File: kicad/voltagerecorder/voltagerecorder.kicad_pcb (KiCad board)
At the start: 2 copper layers, 70.1 x 47.2 mm, 107 parts, among them J1 Conn_02x10_Odd_Even, J2 Phoenix Stecker, J3 Conn_01x08, J4 Conn_01x01_Male, J5 Conn_01x01_Male, J6 Conn_01x01_Male, J7 Conn_01x01_Male, J8 Conn_01x02, J9 USB_C_Receptacle_USB2.0, P1 DM3CS-SF, U1 Opamp_Quad, U2 DCDC_BIPOLAR, U3 L78L12ACUTR, U4 L79L12ACUTR, U5 ADS8638, U6 STM32G473CBT6, U7 L78L12ACUTR, U8 ESP32-C3-WROOM-02, Y1 Crystal_GND23

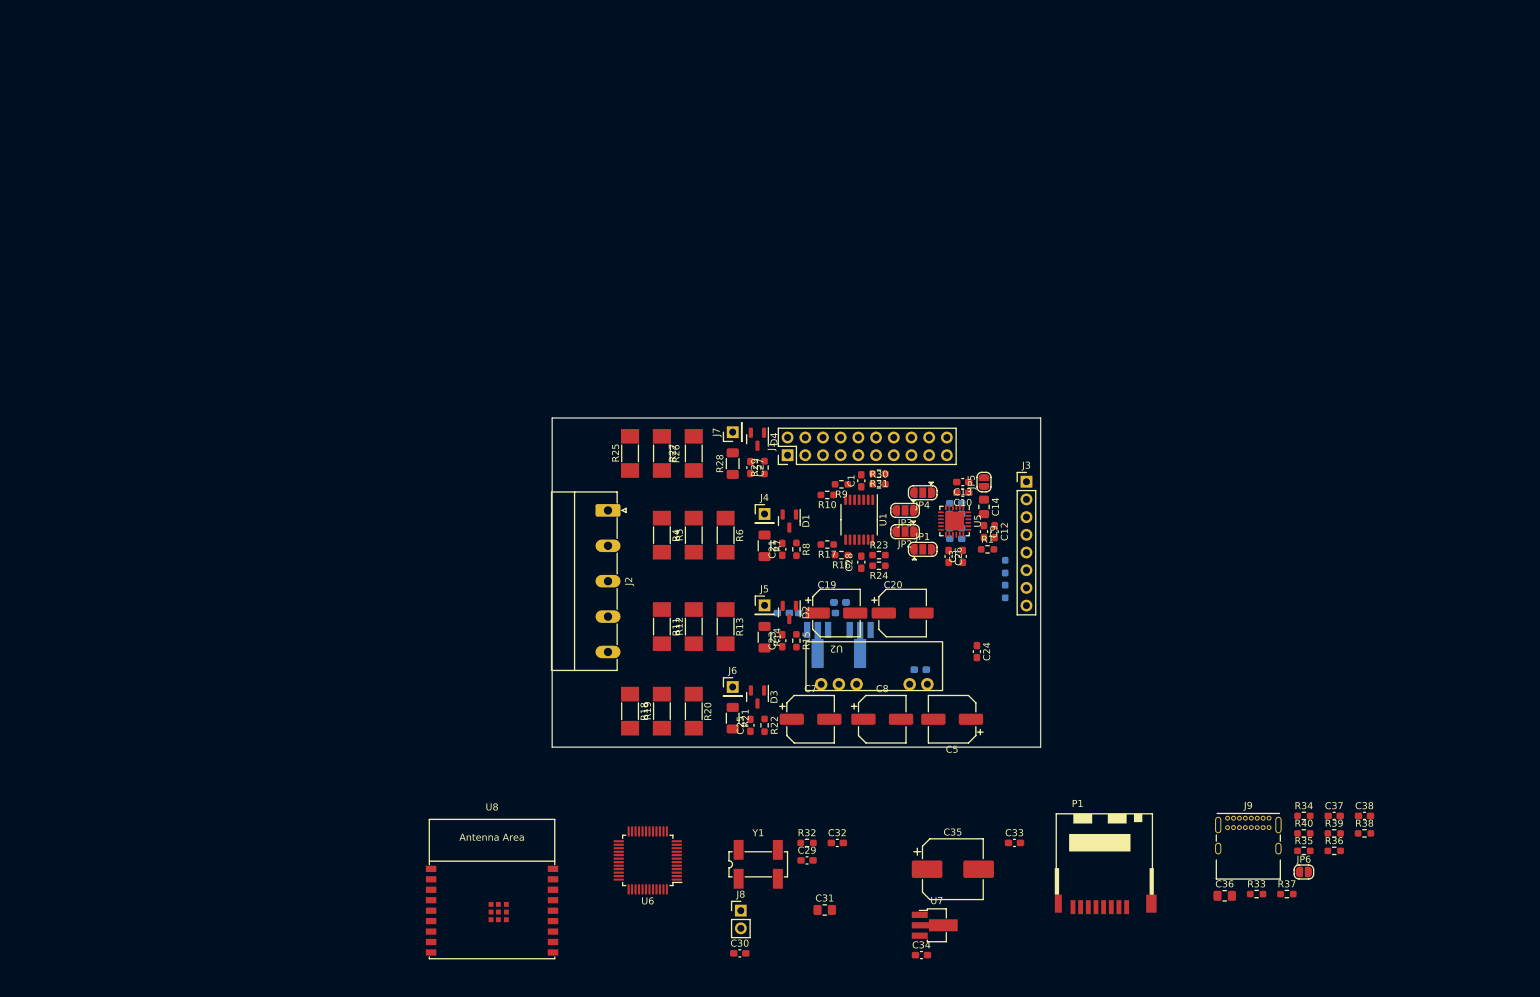
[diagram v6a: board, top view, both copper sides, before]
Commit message: vor entfernung von g4
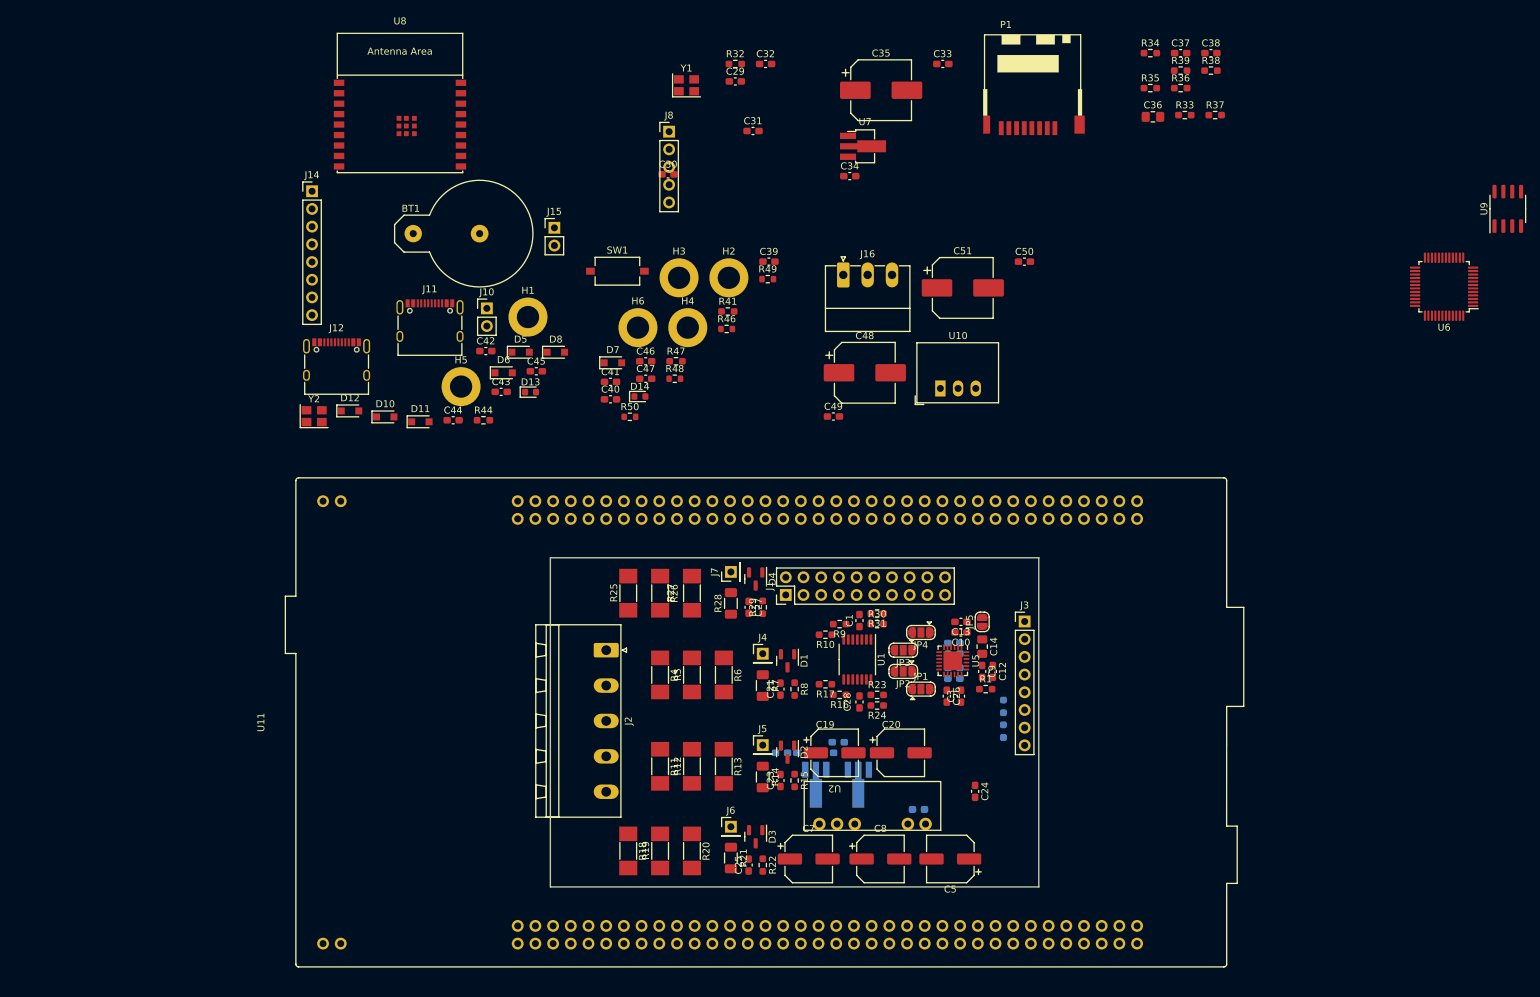
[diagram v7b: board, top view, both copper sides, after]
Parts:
- removed J9: USB_C_Receptacle_USB2.0, Connector_USB:USB_C_Receptacle_GCT_USB4085
- removed JP6: SolderJumper_2_Open, Jumper:SolderJumper-2_P1.3mm_Open_RoundedPad1.0x1.5mm
- removed R40: 15k, Resistor_SMD:R_0603_1608Metric_Pad0.98x0.95mm_HandSolder
- added BT1: Battery_Cell, Battery:BatteryHolder_Keystone_500, F.Cu at (89.8, 52.3)
- added C39: 100n, Capacitor_SMD:C_0603_1608Metric_Pad1.08x0.95mm_HandSolder, F.Cu at (140.8, 56.3)
- added C40: 1u, Capacitor_SMD:C_0603_1608Metric_Pad1.08x0.95mm_HandSolder, F.Cu at (118.1, 76.1)
- added C41: 22pF, Capacitor_SMD:C_0603_1608Metric_Pad1.08x0.95mm_HandSolder, F.Cu at (118.1, 73.5)
- added C42: 22pF, Capacitor_SMD:C_0603_1608Metric_Pad1.08x0.95mm_HandSolder, F.Cu at (100.2, 69.1)
- added C43: 22pF, Capacitor_SMD:C_0603_1608Metric_Pad1.08x0.95mm_HandSolder, F.Cu at (102.4, 75.0)
- added C44: 22pF, Capacitor_SMD:C_0603_1608Metric_Pad1.08x0.95mm_HandSolder, F.Cu at (95.5, 79.1)
- added C45: 100n, Capacitor_SMD:C_0603_1608Metric_Pad1.08x0.95mm_HandSolder, F.Cu at (107.5, 72.0)
- added C46: 10nF, Capacitor_SMD:C_0603_1608Metric_Pad1.08x0.95mm_HandSolder, F.Cu at (123.1, 70.6)
- added C47: 10nF, Capacitor_SMD:C_0603_1608Metric_Pad1.08x0.95mm_HandSolder, F.Cu at (123.1, 73.1)
- added C48: 470u, Capacitor_SMD:CP_Elec_8x10.5, F.Cu at (154.6, 72.2)
- added C49: 10u, Capacitor_SMD:C_0603_1608Metric_Pad1.08x0.95mm_HandSolder, F.Cu at (150.1, 78.5)
- added C50: 10u, Capacitor_SMD:C_0603_1608Metric_Pad1.08x0.95mm_HandSolder, F.Cu at (177.5, 56.3)
- added C51: 470u, Capacitor_SMD:CP_Elec_8x10.5, F.Cu at (168.7, 60.1)
- added D10: D_Zener, Diode_SMD:D_SOD-323_HandSoldering, F.Cu at (85.8, 78.6)
- added D11: D_Zener, Diode_SMD:D_SOD-323_HandSoldering, F.Cu at (90.8, 79.3)
- added D12: D_Zener, Diode_SMD:D_SOD-323_HandSoldering, F.Cu at (80.7, 77.7)
- added D13: RED, Diode_SMD:D_0603_1608Metric, F.Cu at (106.6, 75.0)
- added D14: GREEN, Diode_SMD:D_0603_1608Metric, F.Cu at (122.3, 75.7)
- added D5: D_Zener, Diode_SMD:D_SOD-323_HandSoldering, F.Cu at (105.2, 69.3)
- added D6: D_Zener, Diode_SMD:D_SOD-323_HandSoldering, F.Cu at (102.8, 72.3)
- added D7: D_Zener, Diode_SMD:D_SOD-323_HandSoldering, F.Cu at (118.4, 70.8)
- added D8: D_Zener, Diode_SMD:D_SOD-323_HandSoldering, F.Cu at (110.3, 69.3)
- added H1: MountingHole_Pad, MountingHole:MountingHole_3.2mm_M3_DIN965_Pad, F.Cu at (106.3, 64.3)
- added H2: MountingHole_Pad, MountingHole:MountingHole_3.2mm_M3_DIN965_Pad, F.Cu at (135.1, 58.6)
- added H3: MountingHole_Pad, MountingHole:MountingHole_3.2mm_M3_DIN965_Pad, F.Cu at (127.9, 58.6)
- added H4: MountingHole_Pad, MountingHole:MountingHole_3.2mm_M3_DIN965_Pad, F.Cu at (129.2, 65.8)
- added H5: MountingHole_Pad, MountingHole:MountingHole_3.2mm_M3_DIN965_Pad, F.Cu at (96.7, 74.2)
- added H6: MountingHole_Pad, MountingHole:MountingHole_3.2mm_M3_DIN965_Pad, F.Cu at (122.0, 65.8)
- added J10: Conn_01x02, Connector_PinHeader_2.54mm:PinHeader_1x02_P2.54mm_Vertical, F.Cu at (100.4, 63.0)
- added J11: USB_C_Receptacle_USB2.0, Connector_USB:USB_C_Receptacle_XKB_U262-16XN-4BVC11, F.Cu at (92.2, 66.0)
- added J12: USB_C_Receptacle_USB2.0, Connector_USB:USB_C_Receptacle_XKB_U262-16XN-4BVC11, F.Cu at (78.8, 71.5)
- added J14: Conn_01x08, Connector_PinHeader_2.54mm:PinHeader_1x08_P2.54mm_Vertical, F.Cu at (75.3, 46.2)
- added J15: Conn_01x02, Connector_PinHeader_2.54mm:PinHeader_1x02_P2.54mm_Vertical, F.Cu at (110.0, 51.4)
- added J16: Conn_01x03, Connector_Phoenix_MC:PhoenixContact_MC_1,5_3-G-3.5_1x03_P3.50mm_Horizontal, F.Cu at (151.5, 58.2)
- added R41: 15k, Resistor_SMD:R_0603_1608Metric_Pad0.98x0.95mm_HandSolder, F.Cu at (134.9, 63.4)
- added R44: 10k, Resistor_SMD:R_0603_1608Metric_Pad0.98x0.95mm_HandSolder, F.Cu at (99.9, 79.1)
- added R46: 1M, Resistor_SMD:R_0603_1608Metric, F.Cu at (134.8, 66.0)
- added R47: 10k, Resistor_SMD:R_0603_1608Metric_Pad0.98x0.95mm_HandSolder, F.Cu at (127.5, 70.6)
- added R48: 1M, Resistor_SMD:R_0603_1608Metric, F.Cu at (127.3, 73.1)
- added R49: 1k, Resistor_SMD:R_0603_1608Metric, F.Cu at (140.7, 58.8)
- added R50: 1k, Resistor_SMD:R_0603_1608Metric, F.Cu at (120.9, 78.6)
- added SW1: SW_Push, Button_Switch_SMD:SW_Tactile_SPST_NO_Straight_CK_PTS636Sx25SMTRLFS, F.Cu at (119.1, 57.7)
- added U10: P78E-1000, Converter_DCDC:Converter_DCDC_RECOM_R-78E-0.5_THT, F.Cu at (165.4, 74.5)
- added U11: NUCLEO144-H743ZI, Module:ST_Morpho_Connector_144_STLink, F.Cu at (104.8, 154.2)
- added U9: ESP-PSRAM32, Package_SO:SOIC-8_3.9x4.9mm_P1.27mm, F.Cu at (246.9, 48.7)
- added Y2: 24MHz, Crystal:Crystal_SMD_3225-4Pin_3.2x2.5mm, F.Cu at (75.6, 78.5)
- C24, C29: value 12p -> 100n
- C31: value 10u -> 1u; footprint Capacitor_SMD:C_0805_2012Metric_Pad1.18x1.45mm_HandSolder -> Capacitor_SMD:C_0603_1608Metric_Pad1.08x0.95mm_HandSolder
- C33, C34: value 100n -> 1u
- J2: value Phoenix Stecker -> Conn_01x05; footprint Connector_Phoenix_MC_HighVoltage:PhoenixContact_MC_1,5_5-G-5.08_1x05_P5.08mm_Horizontal -> Connector_Phoenix_MSTB:PhoenixContact_MSTBA_2,5_5-G-5,08_1x05_P5.08mm_Horizontal
- J8: value Conn_01x02 -> Conn_01x05; footprint Connector_PinHeader_2.54mm:PinHeader_1x02_P2.54mm_Vertical -> Connector_PinHeader_2.54mm:PinHeader_1x05_P2.54mm_Vertical
- R3: value nc -> 10k
- Y1: value Crystal_GND23 -> 32.768kHz; footprint Crystal:Crystal_SMD_SeikoEpson_MC306-4Pin_8.0x3.2mm_HandSoldering -> Crystal:Crystal_SMD_3225-4Pin_3.2x2.5mm
- moved U6 140.9 mm to (237.7, 59.9)
- moved U8 113.6 mm to (87.9, 36.5)
- moved C30 112.3 mm to (126.4, 43.8)
- moved C34 112.3 mm to (152.4, 44.0)
- moved U7 112.3 mm to (154.3, 39.7)
- moved C29 112.3 mm to (136.0, 30.4)
- moved C31 112.3 mm to (138.5, 37.5)
- moved Y1 112.3 mm to (129.0, 31.0)
- moved C32 112.3 mm to (140.4, 27.9)
- moved C33 112.3 mm to (165.8, 27.9)
- moved C35 112.3 mm to (156.9, 31.7)
- moved C36 112.3 mm to (196.0, 35.5)
- moved J8 112.3 mm to (126.5, 37.6)
- moved P1 112.3 mm to (178.7, 30.9)
- moved R32 112.3 mm to (136.0, 27.9)
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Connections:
- C24 pad 1: Net-(C24-Pad1) -> +3.3V
- C29 pad 1: Net-(C29-Pad1) -> +3.3V
- C30 pad 1: Net-(C30-Pad1) -> +3.3V
- C32 pad 1: Net-(C31-Pad1) -> /G4_NRST
- C38 pad 1: Net-(C38-Pad1) -> /BUTTON
- J1 pad 1: /IN0_EXT -> GND
- J1 pad 10: unconnected-(J1-Pad10) -> /REF_EXT
- J1 pad 11: +3.3V -> /IN0_EXT
- J1 pad 12: /REF_EXT -> /IN4_EXT
- J1 pad 13: -15V -> /IN1_EXT
- J1 pad 14: +15V -> /IN5_EXT
- J1 pad 15: -12V -> /IN2_EXT
- J1 pad 16: +12V -> /IN6_EXT
- J1 pad 17: +5V -> /IN3_EXT
- J1 pad 18: +5V -> /IN7_EXT
- J1 pad 19: GND -> /G4_PA4
- J1 pad 2: /IN4_EXT -> GND
- J1 pad 20: GND -> /G4_PA5
- J1 pad 3: /IN1_EXT -> +5V
- J1 pad 4: /IN5_EXT -> +5V
- J1 pad 5: /IN2_EXT -> -12V
- J1 pad 6: /IN6_EXT -> +12V
- J1 pad 7: /IN3_EXT -> -15V
- J1 pad 8: /IN7_EXT -> +15V
- J1 pad 9: unconnected-(J1-Pad9) -> +3.3V
- J8 pad 1: unconnected-(J8-Pad1) -> /ESP_EN
- J8 pad 2: GND -> /ESP_BOOT
- P1 pad 1: Net-(P1-Pad1) -> unconnected-(P1-Pad1)
- P1 pad 2: Net-(P1-Pad2) -> /SPI3_NSS
- P1 pad 3: Net-(P1-Pad3) -> /SPI3_MOSI
- P1 pad 5: Net-(P1-Pad5) -> /SPI3_CLK
- P1 pad 7: Net-(P1-Pad7) -> /SPI3_MISO
- P1 pad 8: Net-(P1-Pad8) -> unconnected-(P1-Pad8)
- R1 pad 2: /MISO -> /SPI2_MISO
- R2 pad 1: /CS -> /SPI2_NSS
- R3 pad 2: /CS -> /BOOT0
- R32 pad 1: Net-(C30-Pad1) -> /G4_NRST
- R33 pad 1: Net-(P1-Pad3) -> /SPI3_MOSI
- R34 pad 1: Net-(P1-Pad5) -> /SPI3_CLK
- R35 pad 1: Net-(P1-Pad7) -> /SPI3_MISO
- R36 pad 1: Net-(P1-Pad8) -> /ESP_BOOT
- R37 pad 1: Net-(P1-Pad1) -> /SENSE_5V
- R37 pad 2: +3.3V -> +5V
- R38 pad 1: Net-(P1-Pad2) -> /SPI3_NSS
- R39 pad 1: Net-(C38-Pad1) -> /BUTTON
- R39 pad 2: +5V -> +3.3V
- U5 pad 16: /CS -> /SPI2_NSS
- U5 pad 17: /SCLK -> /SPI2_CLK
- U5 pad 18: /MOSI -> /SPI2_MOSI
- U5 pad 22: /AL_PD -> /ADC_PD
- U6 pad 1: unconnected-(U6-Pad1) -> Net-(BT1-Pad1)
- U6 pad 10: unconnected-(U6-Pad10) -> /QSPI_NSS
- U6 pad 11: unconnected-(U6-Pad11) -> /QSPI_CLK
- U6 pad 12: unconnected-(U6-Pad12) -> /G4_PA4
- U6 pad 13: unconnected-(U6-Pad13) -> /G4_PA5
- U6 pad 14: unconnected-(U6-Pad14) -> /QSPI_IO3
- U6 pad 15: unconnected-(U6-Pad15) -> /QSPI_IO2
- U6 pad 16: unconnected-(U6-Pad16) -> /QSPI_IO1
- U6 pad 17: unconnected-(U6-Pad17) -> /QSPI_IO0
- U6 pad 18: unconnected-(U6-Pad18) -> /SENSE_5V
- U6 pad 19: unconnected-(U6-Pad19) -> GND
- U6 pad 20: unconnected-(U6-Pad20) -> Net-(C31-Pad1)
- U6 pad 21: unconnected-(U6-Pad21) -> +3.3V
- U6 pad 22: unconnected-(U6-Pad22) -> /UART_G4TX_ESPRX
- U6 pad 23: unconnected-(U6-Pad23) -> GND
- U6 pad 24: unconnected-(U6-Pad24) -> +3.3V
- U6 pad 25: unconnected-(U6-Pad25) -> /UART_G4RX_ESPTX
- U6 pad 26: unconnected-(U6-Pad26) -> /SPI2_NSS
- U6 pad 27: unconnected-(U6-Pad27) -> /SPI2_CLK
- U6 pad 28: unconnected-(U6-Pad28) -> /SPI2_MISO
- U6 pad 29: unconnected-(U6-Pad29) -> /SPI2_MOSI
- U6 pad 3: unconnected-(U6-Pad3) -> Net-(C41-Pad1)
- U6 pad 30: unconnected-(U6-Pad30) -> /ADC_PD
- U6 pad 31: unconnected-(U6-Pad31) -> /TRACE-OUT
- U6 pad 32: unconnected-(U6-Pad32) -> /TRACE-IN
- U6 pad 33: unconnected-(U6-Pad33) -> /USB-D-
- U6 pad 34: unconnected-(U6-Pad34) -> /USB-D+
- U6 pad 35: unconnected-(U6-Pad35) -> GND
- U6 pad 36: unconnected-(U6-Pad36) -> +3.3V
- U6 pad 37: unconnected-(U6-Pad37) -> /SWDIO
- U6 pad 38: unconnected-(U6-Pad38) -> /SWDCLK
- U6 pad 39: unconnected-(U6-Pad39) -> /SPI3_NSS
- U6 pad 4: unconnected-(U6-Pad4) -> Net-(C42-Pad1)
- U6 pad 40: unconnected-(U6-Pad40) -> /SPI3_CLK
- U6 pad 41: unconnected-(U6-Pad41) -> /SPI3_MISO
- U6 pad 42: unconnected-(U6-Pad42) -> /SPI3_MOSI
- U6 pad 43: unconnected-(U6-Pad43) -> /USB_CC
- U6 pad 44: unconnected-(U6-Pad44) -> /LED_RED
- U6 pad 45: unconnected-(U6-Pad45) -> /BOOT0
- U6 pad 46: unconnected-(U6-Pad46) -> /LED_GREEN
- U6 pad 47: unconnected-(U6-Pad47) -> GND
- U6 pad 48: unconnected-(U6-Pad48) -> +3.3V
- U6 pad 5: unconnected-(U6-Pad5) -> Net-(C43-Pad1)
- U6 pad 6: unconnected-(U6-Pad6) -> Net-(C44-Pad1)
- U6 pad 7: unconnected-(U6-Pad7) -> /G4_NRST
- U6 pad 8: unconnected-(U6-Pad8) -> /BUTTON
- U6 pad 9: unconnected-(U6-Pad9) -> /ESP_EN
- U8 pad 1: unconnected-(U8-Pad1) -> +3.3V
- U8 pad 10: unconnected-(U8-Pad10) -> GND
- U8 pad 11: unconnected-(U8-Pad11) -> /UART_G4TX_ESPRX
- U8 pad 12: unconnected-(U8-Pad12) -> /UART_G4RX_ESPTX
- U8 pad 2: unconnected-(U8-Pad2) -> /ESP_EN
- U8 pad 7: unconnected-(U8-Pad7) -> +3.3V
- U8 pad 8: unconnected-(U8-Pad8) -> /ESP_BOOT
- Y1 pad 1: Net-(C29-Pad1) -> Net-(C41-Pad1)
- Y1 pad 2: unconnected-(Y1-Pad2) -> GND
- Y1 pad 3: unconnected-(Y1-Pad3) -> Net-(C42-Pad1)
- Y1 pad 4: Net-(C24-Pad1) -> GND

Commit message: G4 entfernt, I2C EEPROM hinzugefügt
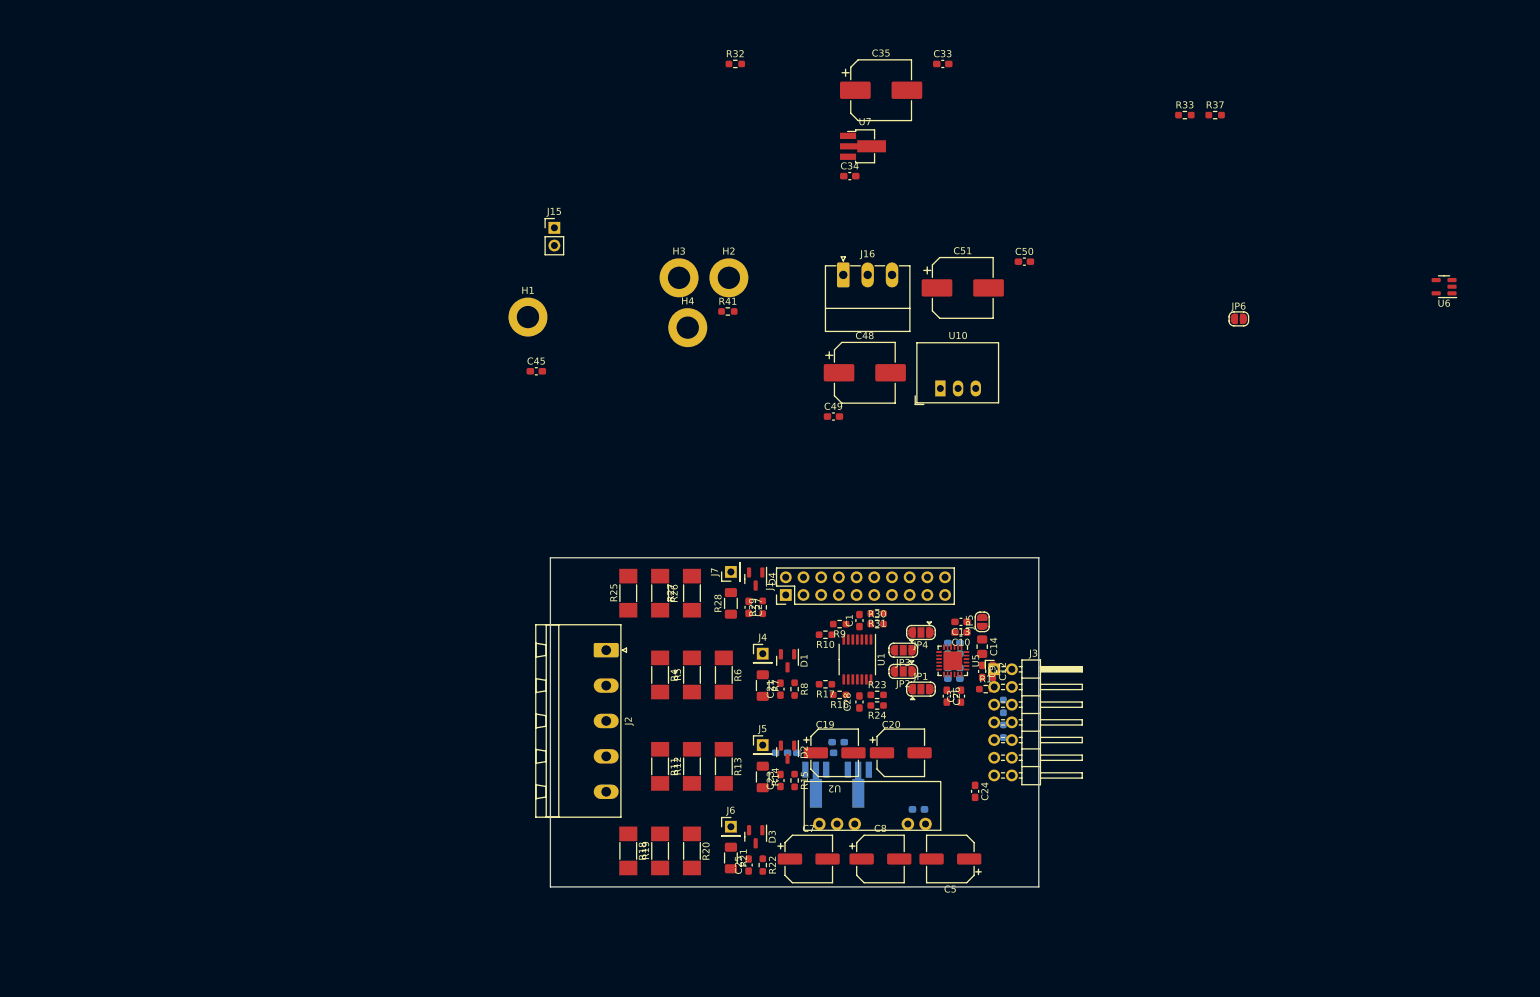
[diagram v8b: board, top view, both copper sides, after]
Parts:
- removed BT1: Battery_Cell, Battery:BatteryHolder_Keystone_500
- removed C29, C30, C32, C37, C38, C39: 100n, Capacitor_SMD:C_0603_1608Metric_Pad1.08x0.95mm_HandSolder
- removed C31, C40: 1u, Capacitor_SMD:C_0603_1608Metric_Pad1.08x0.95mm_HandSolder
- removed C36: 10u, Capacitor_SMD:C_0805_2012Metric_Pad1.18x1.45mm_HandSolder
- removed C41, C42, C43, C44: 22pF, Capacitor_SMD:C_0603_1608Metric_Pad1.08x0.95mm_HandSolder
- removed C46, C47: 10nF, Capacitor_SMD:C_0603_1608Metric_Pad1.08x0.95mm_HandSolder
- removed D10, D11, D12, D5, D6, D7, D8: D_Zener, Diode_SMD:D_SOD-323_HandSoldering
- removed D13: RED, Diode_SMD:D_0603_1608Metric
- removed D14: GREEN, Diode_SMD:D_0603_1608Metric
- removed H5, H6: MountingHole_Pad, MountingHole:MountingHole_3.2mm_M3_DIN965_Pad
- removed J10: Conn_01x02, Connector_PinHeader_2.54mm:PinHeader_1x02_P2.54mm_Vertical
- removed J11, J12: USB_C_Receptacle_USB2.0, Connector_USB:USB_C_Receptacle_XKB_U262-16XN-4BVC11
- removed J14: Conn_01x08, Connector_PinHeader_2.54mm:PinHeader_1x08_P2.54mm_Vertical
- removed J8: Conn_01x05, Connector_PinHeader_2.54mm:PinHeader_1x05_P2.54mm_Vertical
- removed P1: DM3CS-SF, Hirose:HRS_DM3CS-SF
- removed R34, R35, R36, R38, R39, R44, R47: 10k, Resistor_SMD:R_0603_1608Metric_Pad0.98x0.95mm_HandSolder
- removed R46, R48: 1M, Resistor_SMD:R_0603_1608Metric
- removed R49, R50: 1k, Resistor_SMD:R_0603_1608Metric
- removed SW1: SW_Push, Button_Switch_SMD:SW_Tactile_SPST_NO_Straight_CK_PTS636Sx25SMTRLFS
- removed U11: NUCLEO144-H743ZI, Module:ST_Morpho_Connector_144_STLink
- removed U8: ESP32-C3-WROOM-02, Espressif:ESP32-C3-WROOM-02
- removed U9: ESP-PSRAM32, Package_SO:SOIC-8_3.9x4.9mm_P1.27mm
- removed Y1: 32.768kHz, Crystal:Crystal_SMD_3225-4Pin_3.2x2.5mm
- removed Y2: 24MHz, Crystal:Crystal_SMD_3225-4Pin_3.2x2.5mm
- added JP6: SolderJumper_2_Open, Jumper:SolderJumper-2_P1.3mm_Open_RoundedPad1.0x1.5mm, F.Cu at (208.3, 64.5)
- C24: value 100n -> 1u
- J3: value Conn_01x08 -> Conn_02x07_Odd_Even; footprint Connector_PinHeader_2.54mm:PinHeader_1x08_P2.54mm_Vertical -> Connector_PinHeader_2.54mm:PinHeader_2x07_P2.54mm_Horizontal
- U6: value STM32G473CBT6 -> AT24CS08-STUM; footprint Package_QFP:LQFP-48_7x7mm_P0.5mm -> Package_TO_SOT_SMD:SOT-23-5
- moved J3 8.13 mm to (173.2, 114.8)
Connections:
- H1 pad 1: /SHIELD -> GND
- H2 pad 1: /SHIELD -> GND
- H3 pad 1: /SHIELD -> GND
- H4 pad 1: /SHIELD -> GND
- J1 pad 10: /REF_EXT -> /I2C_SDA
- J1 pad 11: /IN0_EXT -> /REF_EXT
- J1 pad 12: /IN4_EXT -> /I2C_SCL
- J1 pad 13: /IN1_EXT -> /IN0_EXT
- J1 pad 14: /IN5_EXT -> /IN4_EXT
- J1 pad 15: /IN2_EXT -> /IN1_EXT
- J1 pad 16: /IN6_EXT -> /IN5_EXT
- J1 pad 17: /IN3_EXT -> /IN2_EXT
- J1 pad 18: /IN7_EXT -> /IN6_EXT
- J1 pad 19: /G4_PA4 -> /IN3_EXT
- J1 pad 20: /G4_PA5 -> /IN7_EXT
- J3 pad 2: /MOSI -> /I2C_SCL
- J3 pad 3: /MISO -> /MOSI
- J3 pad 4: /CS -> /I2C_SDA
- J3 pad 5: /AL_PD -> /MISO
- J3 pad 6: +3.3V -> /AL_PD
- J3 pad 7: +5V -> /CS
- J3 pad 8: GND -> /SENSE_5V
- R3 pad 1: GND -> /I2C_SDA
- R3 pad 2: /BOOT0 -> +3.3V
- R32 pad 1: /G4_NRST -> GND
- R32 pad 2: +3.3V -> Net-(JP6-Pad1)
- R33 pad 1: /SPI3_MOSI -> /I2C_SCL
- U6 pad 1: Net-(BT1-Pad1) -> /I2C_SCL
- U6 pad 2: unconnected-(U6-Pad2) -> GND
- U6 pad 3: Net-(C41-Pad1) -> /I2C_SDA
- U6 pad 4: Net-(C42-Pad1) -> +3.3V
- U6 pad 5: Net-(C43-Pad1) -> Net-(JP6-Pad1)
